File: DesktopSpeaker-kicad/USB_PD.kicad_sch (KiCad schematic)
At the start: 33 parts, among them J4 I2C service, Q1 STL9P3LLH6, Q2 STL9P3LLH6, U11 STUSB4500QTR, U18 TPS26600PWPR, U19 TPS7B8450QWDRBRQ1

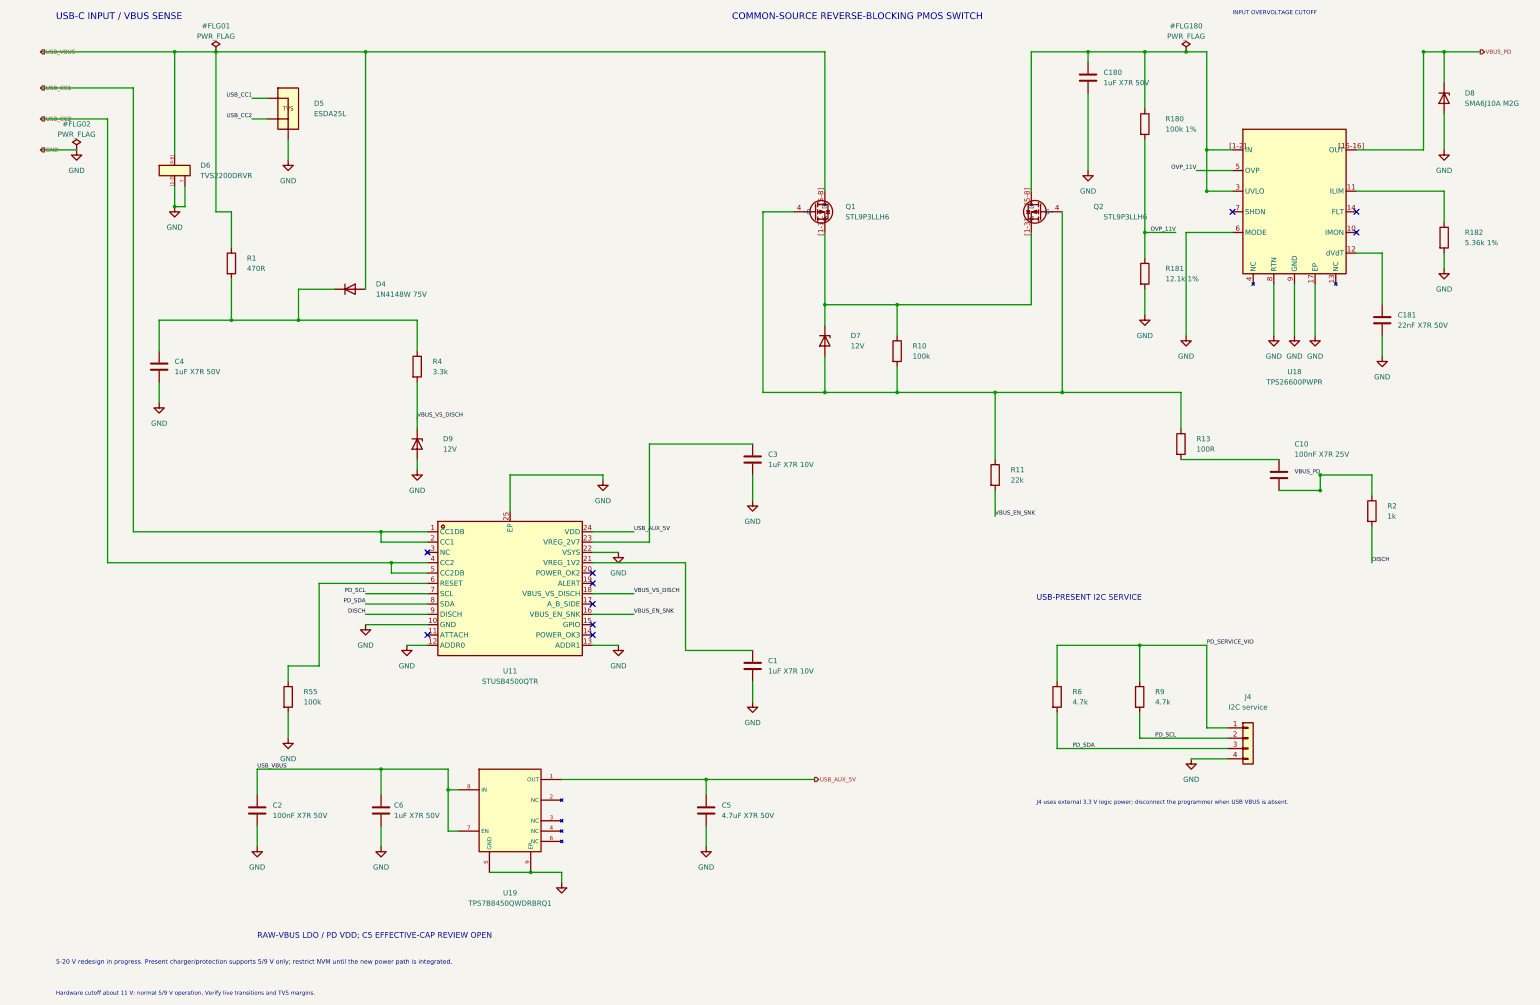
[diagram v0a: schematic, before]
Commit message: Integrate TPS25730D PD and BQ25792 charger into active project (5-20 V); update BOM, plan, handover, preview
Co-Authored-By: Claude Sonnet 5.5 <noreply@anthropic.com>
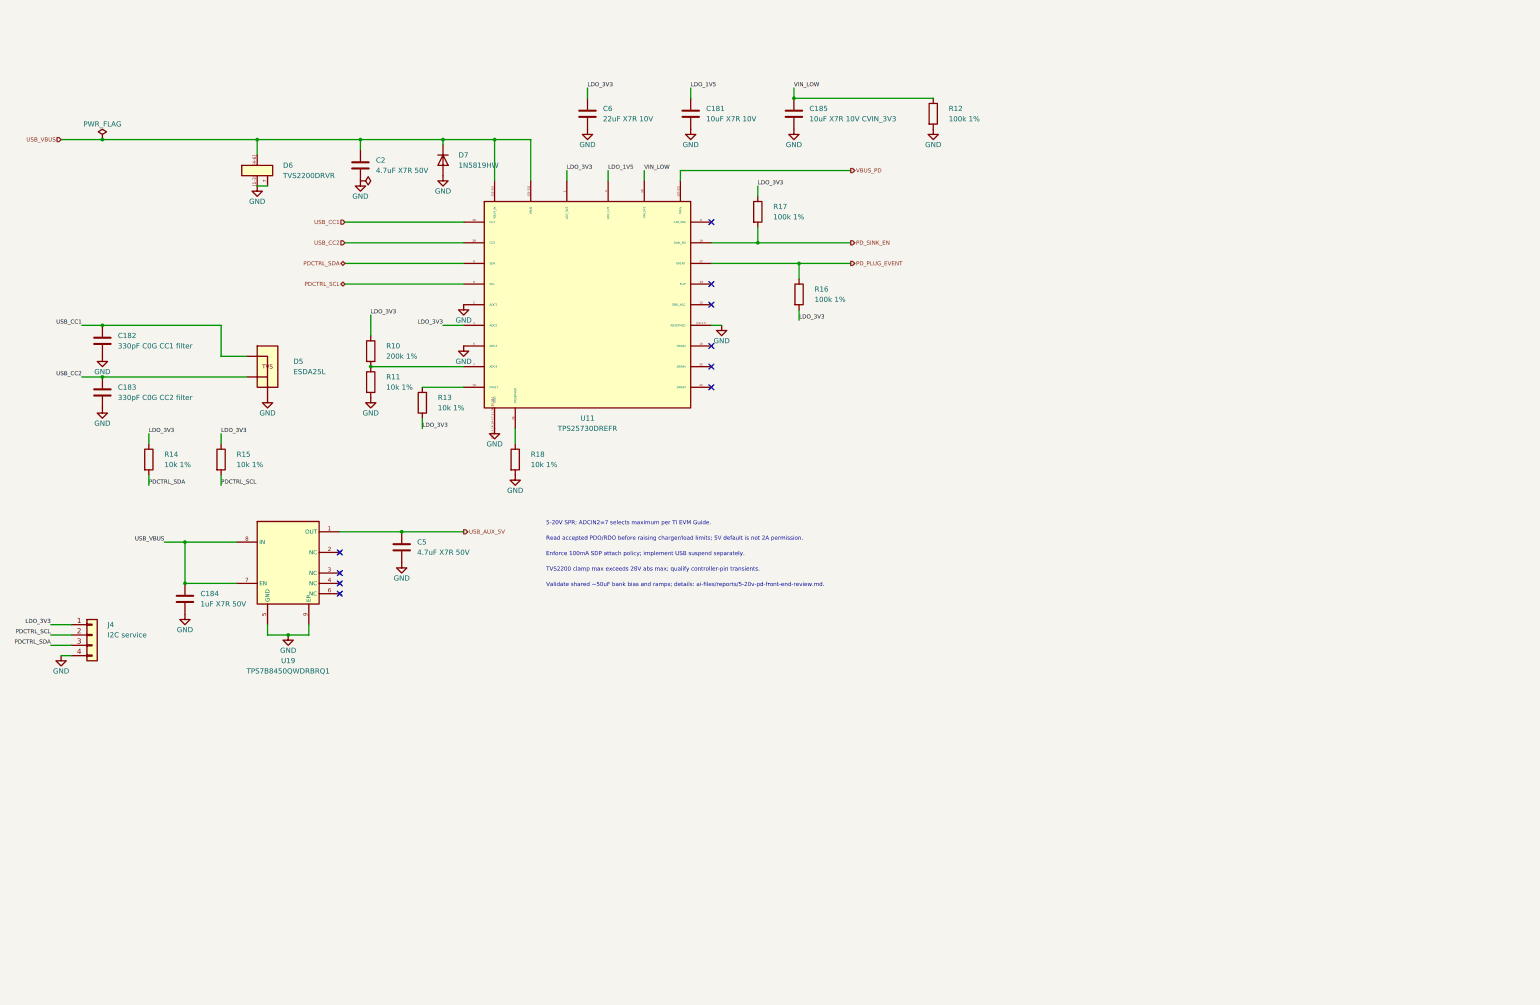
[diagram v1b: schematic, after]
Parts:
- removed C1, C3: 1uF X7R 10V, DesktopSpeaker:PD_C_0603, symbol PD_C:PD_C
- removed C10: 100nF X7R 25V, DesktopSpeaker:PD_C_0805, symbol PD_C:PD_C
- removed C180, C4: 1uF X7R 50V, DesktopSpeaker:PD_C_0805, symbol PD_C:PD_C
- removed D4: 1N4148W 75V, DesktopSpeaker:PD_D_SOD123, symbol PD_DIODE:PD_DIODE
- removed D7, D9: 12V, DesktopSpeaker:BZT52C12-7-F, symbol BZT52C12-7-F:BZT52C12-7-F
- removed D8: SMA6J10A M2G, DesktopSpeaker:SMA6J10A, symbol SMA6J10A:SMA6J10A
- removed Q1, Q2: STL9P3LLH6, DesktopSpeaker:STL9P3LLH6, symbol STL9P3LLH6:STL9P3LLH6
- removed R1: 470R, DesktopSpeaker:PD_R_0603, symbol PD_R:PD_R
- removed R180: 100k 1%, DesktopSpeaker:PD_R_0603, symbol PD_R:PD_R
- removed R181: 12.1k 1%, DesktopSpeaker:PD_R_0603, symbol PD_R:PD_R
- removed R182: 5.36k 1%, DesktopSpeaker:PD_R_0603, symbol PD_R:PD_R
- removed R2: 1k, DesktopSpeaker:PD_R_0603, symbol PD_R:PD_R
- removed R4: 3.3k, DesktopSpeaker:PD_R_1206, symbol PD_R:PD_R
- removed R55: 100k, DesktopSpeaker:PD_R_0603, symbol PD_R:PD_R
- removed R6, R9: 4.7k, DesktopSpeaker:PD_R_0603, symbol PD_R:PD_R
- removed U18: TPS26600PWPR, DesktopSpeaker:TPS26600PWPR, symbol TPS26600PWPR:TPS26600PWPR
- added C182: 330pF C0G CC1 filter, DesktopSpeaker:PD_C_0603, symbol PD_C:PD_C
- added C183: 330pF C0G CC2 filter, DesktopSpeaker:PD_C_0603, symbol PD_C:PD_C
- added C184: 1uF X7R 50V, DesktopSpeaker:PD_C_0805, symbol PD_C:PD_C
- added C185: 10uF X7R 10V CVIN_3V3, DesktopSpeaker:PD_C_0805, symbol PD_C:PD_C
- added D7: 1N5819HW, DesktopSpeaker:PD_D_SOD123, symbol PD_DIODE:PD_DIODE
- added R12, R16, R17: 100k 1%, DesktopSpeaker:PD_R_0603, symbol PD_R:PD_R
- added R14, R15, R18: 10k 1%, DesktopSpeaker:PD_R_0603, symbol PD_R:PD_R
- C181: value 22nF X7R 50V -> 10uF X7R 10V; footprint DesktopSpeaker:PD_C_0603 -> DesktopSpeaker:PD_C_0805; LCSC C21122 -> C32635; LCSC Part C21122 -> C32635; MPN CL10B223KB8NNNC -> CL21B106KPQNNNE
- C2: value 100nF X7R 50V -> 4.7uF X7R 50V; footprint DesktopSpeaker:PD_C_0805 -> DesktopSpeaker:PD_C_1210; LCSC C1711 -> C170099; LCSC Part C1711 -> C170099; MPN CL21B104KBCNNNC -> CL32B475KBUYNNE
- C5: LCSC C51205 -> (none); LCSC Part C51205 -> (none); MPN CL31B475KBHNNNE -> (none); Manufacturer Samsung Electro-Mechanics -> (none)
- C6: value 1uF X7R 50V -> 22uF X7R 10V; LCSC C28323 -> C907991; LCSC Part C28323 -> C907991; MPN CL21B105KBFNNNE -> GRM21BZ71A226ME15L; Manufacturer Samsung Electro-Mechanics -> Murata
- D6: LCSC Part C523793 -> (none); MPN TVS2200DRVR -> TVS2200
- J4: LCSC Part TBD -> (none); MPN TBD -> (none); Manufacturer TBD -> (none)
- R10: value 100k -> 200k 1%; LCSC C14675 -> (none); LCSC Part C14675 -> (none); MPN RC0603FR-07100KL -> (none); Manufacturer YAGEO -> (none)
- R11: value 22k -> 10k 1%; LCSC C114065 -> C98220; LCSC Part C114065 -> C98220; MPN RC0603FR-0722KL -> RC0603FR-0710KL
- R13: value 100R -> 10k 1%; LCSC C105588 -> C98220; LCSC Part C105588 -> C98220; MPN RC0603FR-07100RL -> RC0603FR-0710KL
- U11: value STUSB4500QTR -> TPS25730DREFR; footprint DesktopSpeaker:STUSB4500QTR -> DesktopSpeaker:TPS25730D; symbol STUSB4500QTR:STUSB4500QTR -> TPS25730DREFR:TPS25730DREFR; LCSC Part C2678061 -> C22438973; MPN STUSB4500QTR -> TPS25730DREFR; Manufacturer STMicroelectronics -> Texas Instruments
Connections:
- net PD_SERVICE_VIO is gone; now on net LDO_3V3: J4.1 (Pin_1)
- net VBUS_VS_DISCH is gone; now on an unnamed net: U11.18 (FAULT)
- net GND: now also R11.2, U11.2 (ADC1), U11.5 (ADC3), U11.[11-12,14,16-17,31,34-35,39] (GND), U11.[26-27] (RESERVED), C182.2, C183.2, C184.2, C185.2, D7.2 (A), R12.2, R18.2; no longer U11.10 (GND), U11.12 (ADDR0), U11.13 (ADDR1), U11.22 (VSYS), U11.25 (EP)
- net USB_AUX_5V: no longer U11.24 (VDD)
- net USB_CC1: now also U11.28 (CC1), C182.1; no longer U11.1 (CC1DB), U11.2 (CC1)
- net USB_CC2: now also U11.29 (CC2), C183.1; no longer U11.4 (CC2), U11.5 (CC2DB)
- net USB_VBUS: now also U11.[23-25] (VBUS_IN), U11.[32-33] (VBUS), C184.1, D7.1 (K); no longer C6.1
- net VBUS_PD: now also U11.[20-22] (PPHV)
- net LDO_1V5: now reaches C181.1
- net LDO_1V5: now also U11.4 (LDO_1V5)
- net at R10.2, R11.1: now also U11.7 (ADC4); no longer R13.1
- net LDO_3V3: now reaches R10.1
- net LDO_3V3: now also C6.1, R13.1, U11.1 (LDO_3V3), U11.3 (ADC2), R14.1, R15.1, R16.2, R17.1
- net PD_SINK_EN: now reaches U11.19 (SINK_EN)
- net PD_SINK_EN: now also R17.2
- net DISCH renamed PDCTRL_SCL
- net PDCTRL_SCL: now also J4.2 (Pin_2), R15.2
- removed net PD_SCL: J4.2 (Pin_2), U11.7 (SCL)
- net PD_SDA renamed PDCTRL_SDA
- net PDCTRL_SDA: now also R14.2
- removed net VBUS_EN_SNK: R11.2, U11.16 (VBUS_EN_SNK)
- new net: R18.1, U11.36 (RESERVED)
- new net PD_PLUG_EVENT: R16.1, U11.37 (EVENT)
- new net VIN_LOW: C185.1, R12.1, U11.38 (VIN_3V3)
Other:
- note added: "5-20V SPR; ADCIN2=7 selects maximum per TI EVM Guide."
- note added: "Enforce 100mA SDP attach policy; implement USB suspend separately."
- note added: "Read accepted PDO/RDO before raising charger/load limits; 5V default is not 2A permission."
- note added: "TVS2200 clamp max exceeds 28V abs max; qualify controller-pin transients."
- note added: "Validate shared ~50uF bank bias and ramps; details: ai-files/reports/5-20v-pd-front-end-review.md."
- note removed: "5-20 V redesign in progress. Present charger/protection supports 5/9 V only; restrict NVM until the new power path is integrated."
- note removed: "COMMON-SOURCE REVERSE-BLOCKING PMOS SWITCH"
- note removed: "Hardware cutoff about 11 V: normal 5/9 V operation. Verify live transitions and TVS margins."
- note removed: "INPUT OVERVOLTAGE CUTOFF"
- note removed: "J4 uses external 3.3 V logic power; disconnect the programmer when USB VBUS is absent."
- note removed: "RAW-VBUS LDO / PD VDD; C5 EFFECTIVE-CAP REVIEW OPEN"
- note removed: "USB-C INPUT / VBUS SENSE"
- note removed: "USB-PRESENT I2C SERVICE"
- title: USB-C PD sink: 5V fallback / 9V optional -> USB-C PD 5–20 V SPR — TPS25730D candidate
- moved on the sheet: U11, U19

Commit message: Select R10/C182/C183 parts; add pack, connector and switch options report
Co-Authored-By: Claude Sonnet 5.5 <noreply@anthropic.com>
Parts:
- C182, C183: LCSC Part (none) -> C1578; MPN (none) -> CL10C331JB8NNNC; Manufacturer (none) -> Samsung Electro-Mechanics
- R10: LCSC Part (none) -> C105604; MPN (none) -> RC0603FR-07200KL; Manufacturer (none) -> YAGEO

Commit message: Final integration cleanup: BQ25792 symbol sync, BAT_INT/BATP flags, BOM sweep, plan and open-items list
Co-Authored-By: Claude Sonnet 5.5 <noreply@anthropic.com>
Claude-Session: https://claude.ai/code/session_01N5RHheWSjDFDPbKVD5YVeJ
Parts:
- D6: MPN TVS2200 -> TVS2200DRVR
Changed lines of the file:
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@@
 (symbol (lib_id "TPS25730DREFR:TPS25730DREFR") (at 170.18 101.6 0) (unit 1) (exclude_from_sim no) (in_bom yes) (on_board yes) (dnp no) (property "Reference" "U11" (at 170.18 129.54 0) (effects (font (size 1.27 1.27)))) (property "Value" "TPS25730DREFR" (at 170.18 132.08 0) (effects (font (size 1.27 1.27)))) (property "Footprint" "DesktopSpeaker:TPS25730D" (at 170.18 101.6 0) (effects (font (size 1.27 1.27)) (hide yes))) (property "Datasheet" "${KIPRJMOD}/../ai-files/datasheets/TPS25730.pdf" (at 170.18 101.6 0) (effects (font (size 1.27 1.27)) (hide yes))) (property "Manufacturer" "Texas Instruments" (at 170.18 101.6 0) (effects (font (size 1.27 1.27)) (hide yes))) (property "MPN" "TPS25730DREFR" (at 170.18 101.6 0) (effects (font (size 1.27 1.27)) (hide yes))) (property "LCSC Part" "C22438973" (at 170.18 101.6 0) (effects (font (size 1.27 1.27)) (hide yes))) (pin "28") (pin "29") (pin "8") (pin "9") (pin "2") (pin "3") (pin "5") (pin "7") (pin "18") (pin "6") (pin "19") (pin "37") (pin "13") (pin "10") (pin "[26-27]") (pin "15") (pin "30") (pin "40") (pin "[23-25]") (pin "[32-33]") (pin "1") (pin "4") (pin "38") (pin "[20-22]") (pin "[11-12,14,16-17,31,34-35,39]") (pin "36") (instances (project "DesktopSpeaker" (path "/feda53ed-537d-4f88-9436-c6075776255b/f38b7023-3d53-43ea-b3db-e2c826d87b35" (reference "U11") (unit 1)))))
 (symbol (lib_id "TPS7B8450QWDRBRQ1:TPS7B8450QWDRBRQ1") (at 96.52 165.1 0) (unit 1) (exclude_from_sim no) (in_bom yes) (on_board yes) (dnp no) (property "Reference" "U19" (at 96.52 189.23 0) (effects (font (size 1.27 1.27)))) (property "Value" "TPS7B8450QWDRBRQ1" (at 96.52 191.77 0) (effects (font (size 1.27 1.27)))) (property "Footprint" "DesktopSpeaker:TPS7B8450QWDRBRQ1_WSON-8" (at 96.52 165.1 0) (effects (font (size 1.27 1.27)) (hide yes))) (property "Datasheet" "../ai-files/datasheets/TPS7B84-Q1.pdf" (at 96.52 165.1 0) (effects (font (size 1.27 1.27)) (hide yes))) (property "Manufacturer" "Texas Instruments" (at 96.52 165.1 0) (effects (font (size 1.27 1.27)) (hide yes))) (property "MPN" "TPS7B8450QWDRBRQ1" (at 96.52 165.1 0) (effects (font (size 1.27 1.27)) (hide yes))) (property "LCSC Part" "C3751394" (at 96.52 165.1 0) (effects (font (size 1.27 1.27)) (hide yes))) (pin "8") (pin "7") (pin "1") (pin "2") (pin "3") (pin "4") (pin "6") (pin "5") (pin "9") (instances (project "DesktopSpeaker" (path "/feda53ed-537d-4f88-9436-c6075776255b/f38b7023-3d53-43ea-b3db-e2c826d87b35" (reference "U19") (unit 1)))) (property "Description" "Fixed 5.0 V, 150 mA automotive LDO, WSON-8 DRB with exposed thermal pad" (at 96.52 165.1 0) (effects (font (size 1.27 1.27)) (hide yes))))
-(symbol (lib_id "TVS2200DRVR:TVS2200DRVR") (at 88.9 68.58 0) (unit 1) (exclude_from_sim no) (in_bom yes) (on_board yes) (dnp no) (property "Reference" "D6" (at 95.25 67.31 0) (effects (font (size 1.27 1.27)) (justify left))) (property "Value" "TVS2200DRVR" (at 95.25 69.85 0) (effects (font (size 1.27 1.27)) (justify left))) (property "Footprint" "DesktopSpeaker:TVS2200DRVR" (at 88.9 68.58 0) (effects (font (size 1.27 1.27)) (hide yes))) (property "Datasheet" "${KIPRJMOD}/../ai-files/datasheets/TVS2200.pdf" (at 88.9 68.58 0) (effects (font (size 1.27 1.27)) (hide yes))) (property "Manufacturer" "Texas Instruments" (at 88.9 68.58 0) (effects (font (size 1.27 1.27)) (hide yes))) (property "MPN" "TVS2200" (at 88.9 68.58 0) (effects (font (size 1.27 1.27)) (hide yes))) (pin "[4-6]") (pin "[1-3]") (pin "7") (instances (project "DesktopSpeaker" (path "/feda53ed-537d-4f88-9436-c6075776255b/f38b7023-3d53-43ea-b3db-e2c826d87b35" (reference "D6") (unit 1)))))
+(symbol (lib_id "TVS2200DRVR:TVS2200DRVR") (at 88.9 68.58 0) (unit 1) (exclude_from_sim no) (in_bom yes) (on_board yes) (dnp no) (property "Reference" "D6" (at 95.25 67.31 0) (effects (font (size 1.27 1.27)) (justify left))) (property "Value" "TVS2200DRVR" (at 95.25 69.85 0) (effects (font (size 1.27 1.27)) (justify left))) (property "Footprint" "DesktopSpeaker:TVS2200DRVR" (at 88.9 68.58 0) (effects (font (size 1.27 1.27)) (hide yes))) (property "Datasheet" "${KIPRJMOD}/../ai-files/datasheets/TVS2200.pdf" (at 88.9 68.58 0) (effects (font (size 1.27 1.27)) (hide yes))) (property "Manufacturer" "Texas Instruments" (at 88.9 68.58 0) (effects (font (size 1.27 1.27)) (hide yes))) (property "MPN" "TVS2200DRVR" (at 88.9 68.58 0) (effects (font (size 1.27 1.27)) (hide yes))) (pin "[4-6]") (pin "[1-3]") (pin "7") (instances (project "DesktopSpeaker" (path "/feda53ed-537d-4f88-9436-c6075776255b/f38b7023-3d53-43ea-b3db-e2c826d87b35" (reference "D6") (unit 1)))))
 (symbol (lib_id "ESDA25L:ESDA25L") (at 91.44 116.84 0) (unit 1) (exclude_from_sim no) (in_bom yes) (on_board yes) (dnp no) (property "Reference" "D5" (at 97.79 115.57 0) (effects (font (size 1.27 1.27)) (justify left))) (property "Value" "ESDA25L" (at 97.79 118.11 0) (effects (font (size 1.27 1.27)) (justify left))) (property "Footprint" "DesktopSpeaker:ESDA25L" (at 91.44 116.84 0) (effects (font (size 1.27 1.27)) (hide yes))) (property "Datasheet" "${KIPRJMOD}/../ai-files/datasheets/ESDAL-ST.pdf" (at 91.44 116.84 0) (effects (font (size 1.27 1.27)) (hide yes))) (property "Manufacturer" "STMicroelectronics" (at 91.44 116.84 0) (effects (font (size 1.27 1.27)) (hide yes))) (property "MPN" "ESDA25L" (at 91.44 116.84 0) (effects (font (size 1.27 1.27)) (hide yes))) (property "LCSC Part" "C95343" (at 91.44 116.84 0) (effects (font (size 1.27 1.27)) (hide yes))) (pin "1") (pin "2") (pin "3") (instances (project "DesktopSpeaker" (path "/feda53ed-537d-4f88-9436-c6075776255b/f38b7023-3d53-43ea-b3db-e2c826d87b35" (reference "D5") (unit 1)))))
 (symbol (lib_id "PD_C:PD_C") (at 114.3 67.31 0) (unit 1) (exclude_from_sim no) (in_bom yes) (on_board yes) (dnp no) (property "Reference" "C2" (at 118.11 66.04 0) (effects (font (size 1.27 1.27)) (justify left))) (property "Value" "4.7uF X7R 50V" (at 118.11 68.58 0) (effects (font (size 1.27 1.27)) (justify left))) (property "Footprint" "DesktopSpeaker:PD_C_1210" (at 114.3 67.31 0) (effects (font (size 1.27 1.27)) (hide yes))) (property "Datasheet" "" (at 114.3 67.31 0) (effects (font (size 1.27 1.27)) (hide yes))) (pin "1") (pin "2") (instances (project "DesktopSpeaker" (path "/feda53ed-537d-4f88-9436-c6075776255b/f38b7023-3d53-43ea-b3db-e2c826d87b35" (reference "C2") (unit 1)))) (property "Manufacturer" "Samsung Electro-Mechanics" (at 114.3 67.31 0) (effects (font (size 1.27 1.27)) (hide yes))) (property "MPN" "CL32B475KBUYNNE" (at 114.3 67.31 0) (effects (font (size 1.27 1.27)) (hide yes))) (property "LCSC Part" "C170099" (at 114.3 67.31 0) (effects (font (size 1.27 1.27)) (hide yes))) (property "LCSC" "C170099" (at 114.3 67.31 0) (effects (font (size 1.27 1.27)) (hide yes))) (property "Datasheet" "https://product.samsungsem.com/mlcc/CL32B475KBUYNN.do" (at 114.3 67.31 0) (effects (font (size 1.27 1.27)) (hide yes))))

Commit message: Repackage passives to 0402/0805 hand-solder footprints; update BOM and flags
Co-Authored-By: Claude Sonnet 5.5 <noreply@anthropic.com>
Claude-Session: https://claude.ai/code/session_01N5RHheWSjDFDPbKVD5YVeJ
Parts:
- C181, C184, C185, C6: footprint DesktopSpeaker:PD_C_0805 -> DesktopSpeaker:C_0805_2012Metric_Pad1.18x1.45mm_HandSolder
- C182, C183: footprint DesktopSpeaker:PD_C_0603 -> DesktopSpeaker:C_0402_1005Metric_Pad0.74x0.62mm_HandSolder; LCSC Part C1578 -> (none); MPN CL10C331JB8NNNC -> GRM1555C1H331JA01D; Manufacturer Samsung Electro-Mechanics -> Murata
- C2: footprint DesktopSpeaker:PD_C_1210 -> DesktopSpeaker:C_0805_2012Metric_Pad1.18x1.45mm_HandSolder; LCSC C170099 -> (none); LCSC Part C170099 -> (none); MPN CL32B475KBUYNNE -> C2012X7R1H475K125AC; Manufacturer Samsung Electro-Mechanics -> TDK
- C5: footprint DesktopSpeaker:PD_C_1206 -> DesktopSpeaker:C_0805_2012Metric_Pad1.18x1.45mm_HandSolder; MPN (none) -> C2012X7R1H475K125AC; Manufacturer (none) -> TDK
- R10: footprint DesktopSpeaker:PD_R_0603 -> DesktopSpeaker:R_0402_1005Metric_Pad0.72x0.64mm_HandSolder; LCSC Part C105604 -> (none); MPN RC0603FR-07200KL -> RC0402FR-07200KL; Manufacturer YAGEO -> Yageo
- R11, R13, R14, R15, R18: footprint DesktopSpeaker:PD_R_0603 -> DesktopSpeaker:R_0402_1005Metric_Pad0.72x0.64mm_HandSolder; LCSC C98220 -> C60490; LCSC Part C98220 -> C60490; MPN RC0603FR-0710KL -> RC0402FR-0710KL; Manufacturer YAGEO -> Yageo
- R12, R16, R17: footprint DesktopSpeaker:PD_R_0603 -> DesktopSpeaker:R_0402_1005Metric_Pad0.72x0.64mm_HandSolder; LCSC C14675 -> C60491; LCSC Part C14675 -> C60491; MPN RC0603FR-07100KL -> RC0402FR-07100KL; Manufacturer YAGEO -> Yageo
